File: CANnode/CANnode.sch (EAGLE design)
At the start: 245 parts, among them IC1 ISO1050DUB, IC2 ISO1050DUB, Q1 FDV302P, Q3 FDV302P, U1 LM324PW, U10 FT2232HL, U11 93LC56C-I/SN, U2 TPS70445_PWP_24, U3 LM324PW, U4 LM324PW, U5 LM324PW, U6 LM324PW, U7 RM42L432_PZ_100RM42L432_PZ_100, U8 LM324PW, U9 XC2C32A-6CP56C, X1 AS14-35, Y1 12M

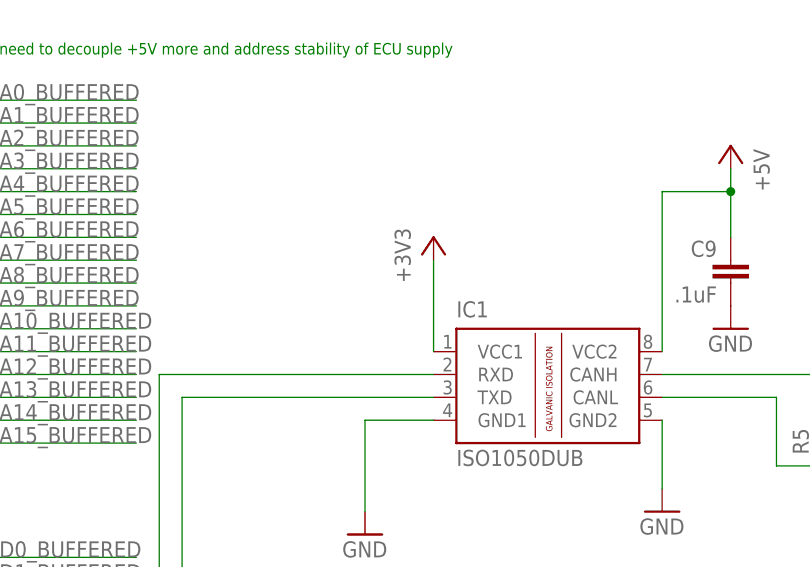
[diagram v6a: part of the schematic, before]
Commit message: Fished wiring+3V3 and started wiring can components
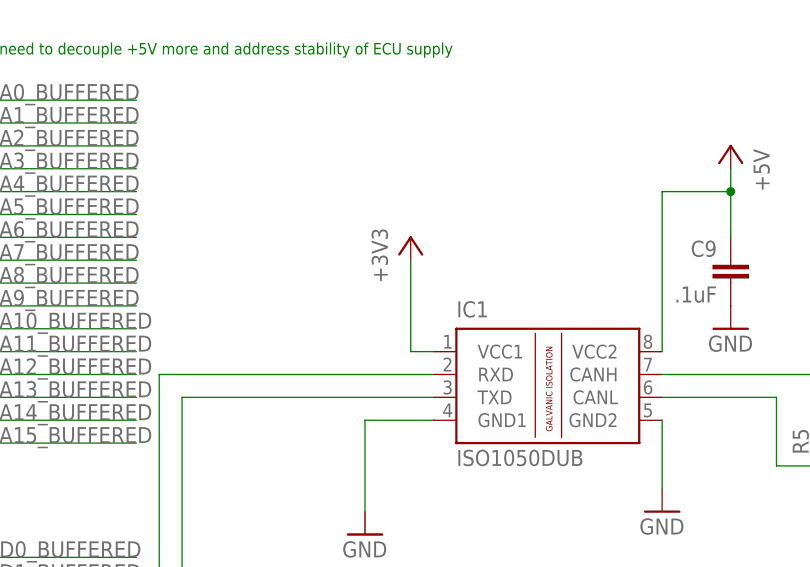
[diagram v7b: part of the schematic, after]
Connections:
- net +3V3: now also IC1.VCC1
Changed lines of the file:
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@@
 <instance part="C7" gate="G$1" x="482.6" y="-25.4"/>
 <instance part="+3V4" gate="G$1" x="477.52" y="-17.78"/>
-<instance part="+3V5" gate="G$1" x="480.06" y="45.72"/>
+<instance part="+3V5" gate="G$1" x="477.52" y="45.72"/>
 <instance part="GND43" gate="1" x="2.54" y="-101.6"/>
 <instance part="GND44" gate="1" x="12.7" y="-111.76"/>
@@
 </segment>
 <segment>
-<pinref part="+3V5" gate="G$1" pin="+3V3"/>
-<wire x1="480.06" y1="33.02" x2="480.06" y2="43.18" width="0.1524" layer="91"/>
-</segment>
-<segment>
 <pinref part="+3V10" gate="G$1" pin="+3V3"/>
 <wire x1="274.32" y1="-58.42" x2="274.32" y2="-66.04" width="0.1524" layer="91"/>
@@
 <junction x="271.78" y="-355.6"/>
 </segment>
+<segment>
+<pinref part="+3V5" gate="G$1" pin="+3V3"/>
+<wire x1="477.52" y1="43.18" x2="477.52" y2="33.02" width="0.1524" layer="91"/>
+<wire x1="477.52" y1="33.02" x2="480.06" y2="33.02" width="0.1524" layer="91"/>
+<pinref part="IC1" gate="G$1" pin="VCC1"/>
+</segment>
 </net>

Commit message: Focused on power positioning and some routing. Finished 5V_IN from connector and +5V to power supply. Placed caps for 3V3 and 1V2 around RM42. Placed and routed crystal.
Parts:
- added C73: 100nF, rcl:C-EUC0402
- added C74: 100nF, eagle-ltspice:CC0402
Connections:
- net +1V2: no longer C19.1
- net +3V3: now also C19.1, C73.1, U7.VCCAD/ADREFHI, U7.VCCIO_5
- net +5V: now also C74.1
- net GND: now also C73.2, C74.2, U7.VSSAD/ADREFLO
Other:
- note removed: "I can find no trace of 30pF capacitors in the manual"
- moved on the sheet: C19
